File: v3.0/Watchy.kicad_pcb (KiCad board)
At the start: 2 copper layers, 33.8 x 46 mm, 78 parts, among them J1 FPC24(0.5MM), J2 Conn_01x06, J3 Battery, J5 Conn_01x06, M1 Vibration_Motor, Q1 AO3400A, Q4 CJ2301, Q5 S8050, SW1 BTN, SW2 BTN, SW3 BTN, SW4 BTN, U1 CH340X, U2 ME6211C33M5G-N, U3 USBLC6-2P6, U4 BMA423, U5 TP4054, U6 PCF8563BS, U7 ESP32-S3, U8 SR2HARU, Y1 32.768KHz, Y3 40MHZ

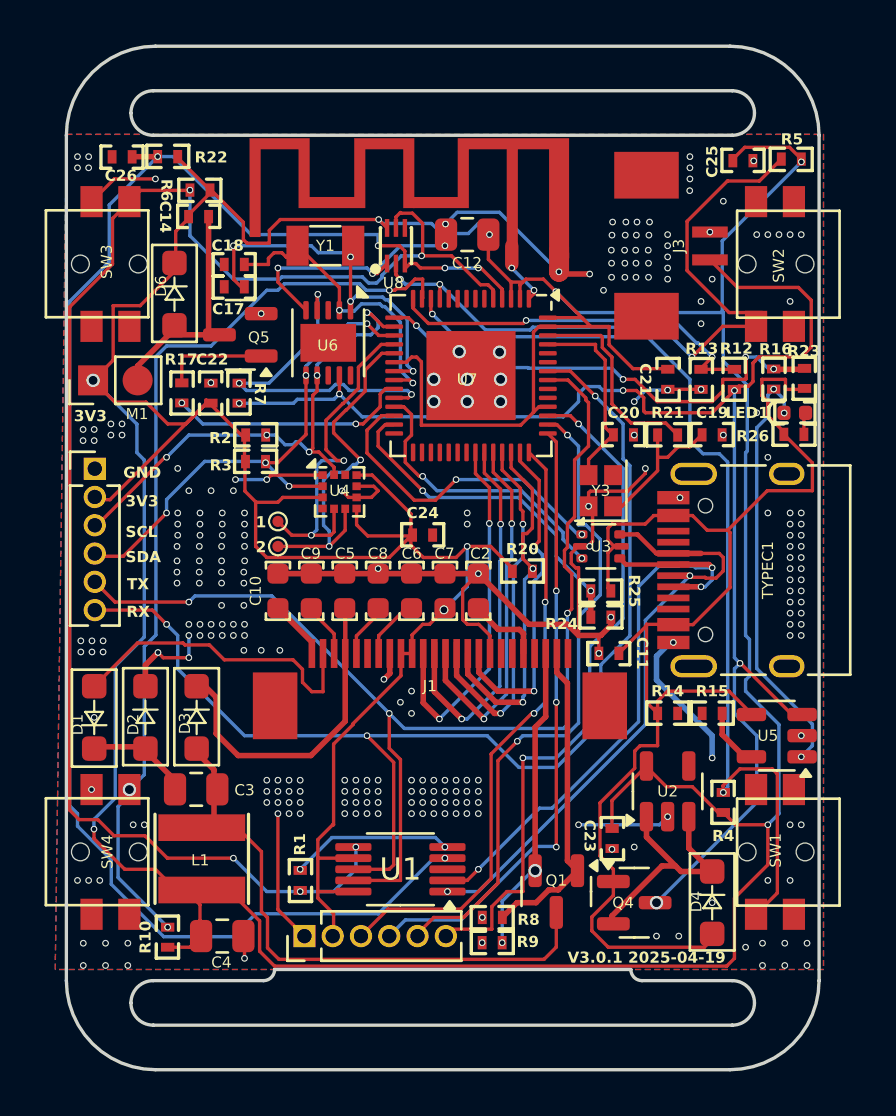
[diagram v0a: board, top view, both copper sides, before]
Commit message: delete R16,R23
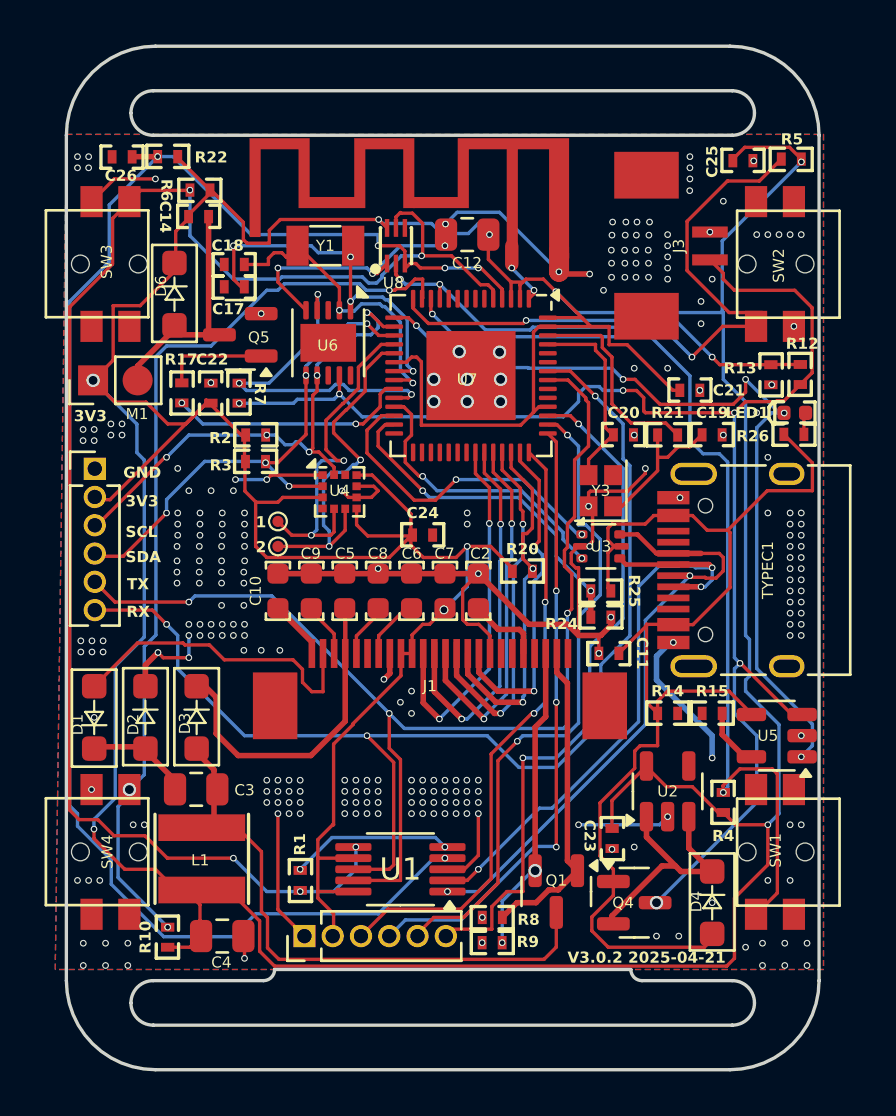
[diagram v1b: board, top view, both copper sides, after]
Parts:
- removed R16: 100K, Watchy:R0402-Frame
- removed R23: 51K, Watchy:R0402-Frame
- moved R13 3.14 mm to (100.3, 84.9)
- moved R12 2.97 mm to (101.7, 84.9)
- moved C21 1.12 mm to (96.7, 85.6), turned to 0 degrees
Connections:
- LED1 pad 1: Net-(LED1-K) -> STAT
- U5 pad 1: Net-(LED1-K) -> STAT
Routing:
- net Net-(LED1-K): track 19.3 -> 0.00 mm, vias 3 -> 0
- net STAT: track 22.1 -> 38.5 mm, vias 4 -> 5
- net VBUS: track 58.7 -> 53.7 mm
- net ADC: track 17.1 -> 19.0 mm
- net +3V3: track 250.7 -> 251.5 mm
- net +BATT: track 67.1 -> 66.3 mm
- net GND: track 90.5 -> 90.9 mm, vias 273 -> 274
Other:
- board text added: "V3.0.2 2025-04-21"
- board text removed: "V3.0.1 2025-04-19"
